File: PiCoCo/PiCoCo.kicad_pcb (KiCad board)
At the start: 2 copper layers, 98 x 65.2 mm, 42 parts, among them P1 COCO-CART, Q2 2N7002, U1 Pico 2, U10 SN74LVC8T245DW, U11 SN74LVC245AD, U12 SN74LVC245AD, U13 SN74LVC245AD, U14 AMS1117-3.3, U15 SN74LVC1G11

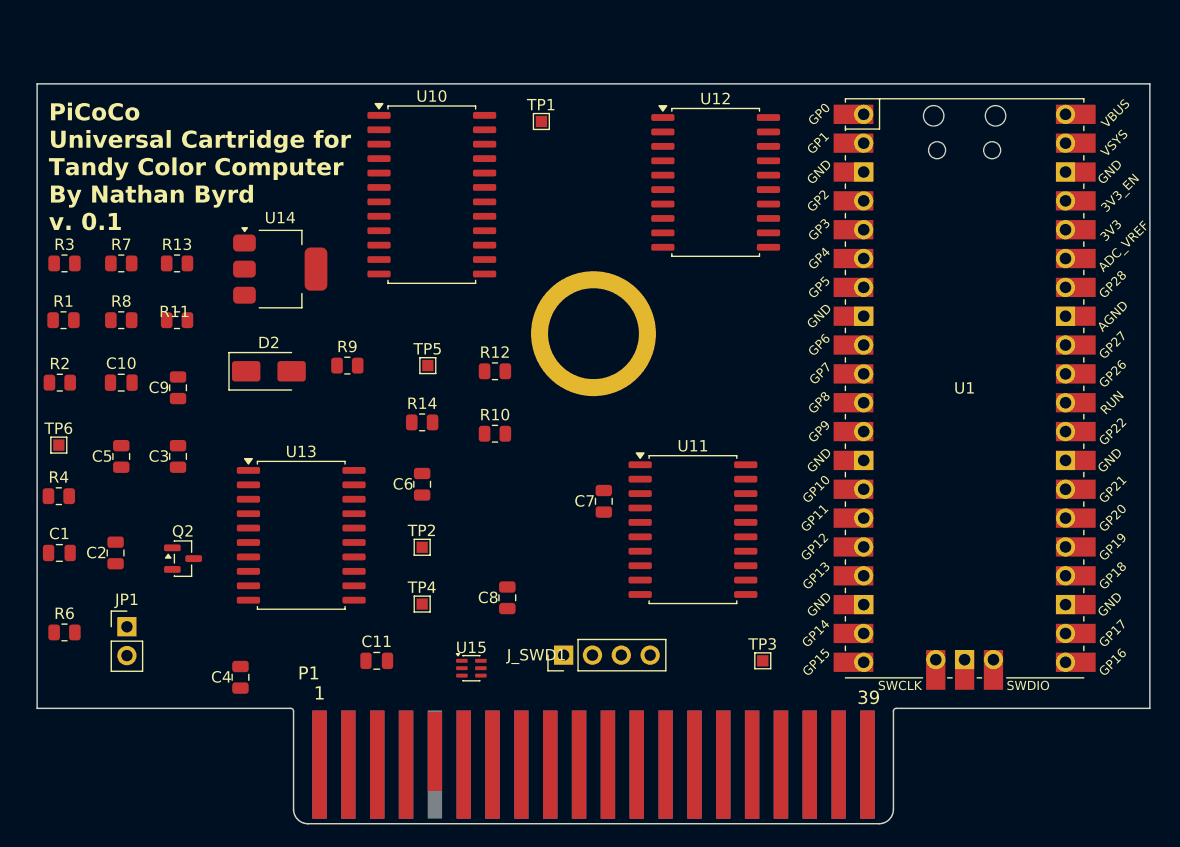
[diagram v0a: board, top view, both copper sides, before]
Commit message: kicad: v2.3 placement, antenna and HDMI rule areas, silkscreen
Placement table for the v2.3 refresh (Pico-Carrier module, LVC245/LVC00
buffers, sound stage, JP2/JP3, fiducials), antenna and HDMI-reserve
keepout zones, and silkscreen texts via place_pcb.py's add_board_extras().

Deviations from the task-4 brief, found via measured courtyard/pad
geometry after placement (not guessed):
- U14/C1 moved +/-3mm in x; D2's 7mm-wide courtyard didn't fit the
  brief's gap between them.
- Decoupling caps C4/C6/C7/C8 moved from y=84.0 to y=83.0; the buffer
  ICs' courtyard starts at y=85.35, so y=84.0 clipped it by ~0.35mm.
- JP3/C10 moved +8mm in x; at the brief's x=152 both sat inside U1's
  courtyard (ends x=155.52) and the antenna keepout (x 150.6..155.6).
- Sound stage (R19/C13/R20/C14/R21/R22/C15/TP7) regridded to 2 rows x
  4 cols right of U13 (courtyard ends x=187.93); the brief's single row
  put three parts inside both U13's courtyard and FID2's fiducial
  clearance.
- FID1 relocated twice (102.6/47.2 -> inside U1's own pad clearance;
  102.6/70.0 -> inside C12's 10.5x8.8mm courtyard) to 114.0/76.0, the
  first open spot found between C12 and R4/C2's row.

Known unresolved issue, needs a ruling: P1's MTG1 mounting-hole pad
(11mm pad / 8mm drill, baked into the shared COCO-CART footprint) sits
inside the v2.3 module's body corner regardless of U1's rotation (90 or
270), producing 3 hole_to_hole violations, several antenna-keepout
item_not_allowed hits, and ~11 net-shorting flags against U1's nearby
pins. This predates the v2.3 horizontal-module layout and can't be
fixed by nudging PLACEMENT; it needs either relocating MTG1 in the
footprint or accepting no mounting screw at that corner.

Also present, out of scope for this script: ~76 shorting_items flagged
between adjacent castellated pins on U1 itself (e.g. D0/D1) -- inherent
to the Pico-Carrier footprint's own pad-to-pad clearance vs. the
board's DRC clearance rule, a Task 1 footprint concern, not a
placement issue. 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
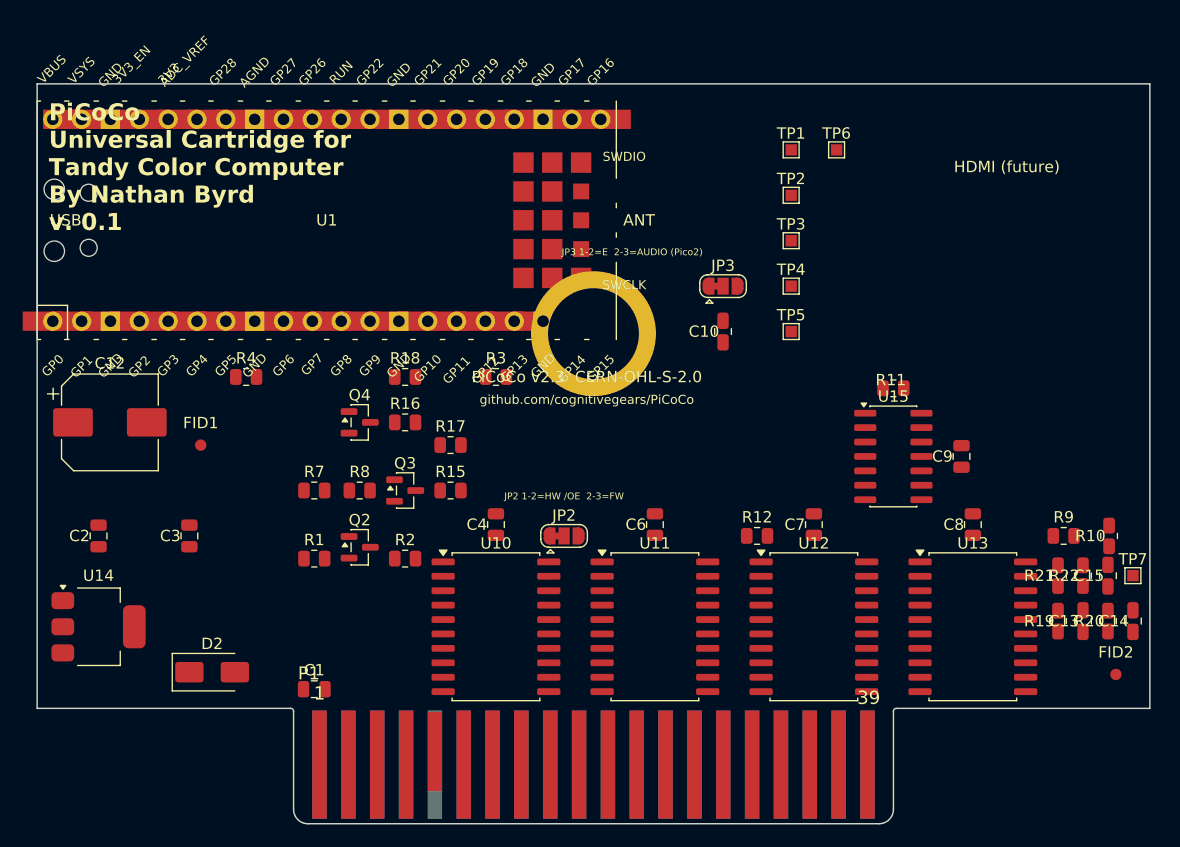
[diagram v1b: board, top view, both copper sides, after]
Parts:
- removed C11: 10uF, Capacitor_SMD:C_0805_2012Metric
- removed C5: 100nF, Capacitor_SMD:C_0805_2012Metric
- removed JP1: CART_EN, Connector_PinHeader_2.54mm:PinHeader_1x02_P2.54mm_Vertical
- removed J_SWD1: SWD, Connector_PinHeader_2.54mm:PinHeader_1x04_P2.54mm_Vertical
- removed R13, R14: 100, Resistor_SMD:R_0805_2012Metric
- removed R6: 4.7k, Resistor_SMD:R_0805_2012Metric
- added C12: 1000uF 6.3V, Capacitor_SMD:CP_Elec_8x10, F.Cu at (106.0, 74.0)
- added C13: 10nF, Capacitor_SMD:C_0805_2012Metric, F.Cu at (191.7, 91.5)
- added C14: 10nF, Capacitor_SMD:C_0805_2012Metric, F.Cu at (196.1, 91.5)
- added C15: 100nF, Capacitor_SMD:C_0805_2012Metric, F.Cu at (193.9, 87.5)
- added FID1: FID, Fiducial:Fiducial_1mm_Mask2mm, F.Cu at (114.0, 76.0)
- added FID2: FID, Fiducial:Fiducial_1mm_Mask2mm, F.Cu at (194.6, 96.2)
- added JP2: U10_OE_SEL, Jumper:SolderJumper-3_P1.3mm_Bridged12_RoundedPad1.0x1.5mm, F.Cu at (146.0, 84.0)
- added JP3: P34_SEL, Jumper:SolderJumper-3_P1.3mm_Bridged12_RoundedPad1.0x1.5mm, F.Cu at (160.0, 62.0)
- added Q3: 2N7002, Package_TO_SOT_SMD:SOT-23, F.Cu at (132.0, 80.0)
- added Q4: 2N7002, Package_TO_SOT_SMD:SOT-23, F.Cu at (128.0, 74.0)
- added R15: 100, Resistor_SMD:R_0805_2012Metric, F.Cu at (136.0, 80.0)
- added R16: 100, Resistor_SMD:R_0805_2012Metric, F.Cu at (132.0, 74.0)
- added R17: 100k, Resistor_SMD:R_0805_2012Metric, F.Cu at (136.0, 76.0)
- added R18: 100k, Resistor_SMD:R_0805_2012Metric, F.Cu at (132.0, 70.0)
- added R19: 1k, Resistor_SMD:R_0805_2012Metric, F.Cu at (189.5, 91.5)
- added R20: 1k, Resistor_SMD:R_0805_2012Metric, F.Cu at (193.9, 91.5)
- added R21: 2.2k, Resistor_SMD:R_0805_2012Metric, F.Cu at (189.5, 87.5)
- added R22: 1k, Resistor_SMD:R_0805_2012Metric, F.Cu at (191.7, 87.5)
- added TP7: SND_CART, TestPoint:TestPoint_Pad_1.0x1.0mm, F.Cu at (196.1, 87.5)
- TP5: value E_B -> E_BUF
- U1: value Pico 2 -> Pico 2 / RP2350B-Plus-W; footprint PiCoCo:RPi_Pico_SMD_TH -> PiCoCo:Pico-Carrier
- U10: value SN74LVC8T245DW -> SN74LVC245A; footprint Package_SO:SOIC-24W_7.5x15.4mm_P1.27mm -> Package_SO:SOIC-20W_7.5x12.8mm_P1.27mm
- U11, U12, U13: value SN74LVC245AD -> SN74LVC245A
- U15: value SN74LVC1G11 -> SN74LVC00A; footprint Package_TO_SOT_SMD:SOT-363_SC-70-6 -> Package_SO:SOIC-14_3.9x8.7mm_P1.27mm
- moved TP6 73.3 mm to (170.0, 50.0)
- moved C9 69.3 mm to (181.0, 77.0)
- moved R9 64.8 mm to (190.0, 84.0)
- moved R11 63.4 mm to (175.0, 71.0)
- moved U13 59.7 mm to (182.0, 92.0)
- moved U1 58.1 mm to (125.1, 56.2), turned to 90 degrees
- moved R10 54.8 mm to (194.0, 84.0), turned to 90 degrees
- moved C10 53.2 mm to (160.0, 66.0), turned to 90 degrees
- moved TP2 44.9 mm to (166.0, 54.0)
- moved TP4 42.9 mm to (166.0, 62.0)
- moved U15 41.6 mm to (175.0, 77.0)
- moved C8 41.5 mm to (182.0, 83.0)
- moved U12 40.1 mm to (168.0, 92.0)
- moved R3 39.3 mm to (140.0, 70.0)
- moved U10 38.5 mm to (140.0, 92.0)
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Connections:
- net A0_B renamed A0_BUF
- net A10_B renamed A10_BUF
- net A11_B renamed A11_BUF
- net A12_B renamed A12_BUF
- net A13_B renamed A13_BUF
- net A1_B renamed A1_BUF
- net A2_B renamed A2_BUF
- net A3_B renamed A3_BUF
- net A4_B renamed A4_BUF
- net A5_B renamed A5_BUF
- net A6_B renamed A6_BUF
- net A7_B renamed A7_BUF
- net A8_B renamed A8_BUF
- net A9_B renamed A9_BUF
- P1 pad 35: unconnected-(P1-SND-Pad35) -> SND_CART
- R9 pad 1: RESET_DBG -> RESET_BUF
- TP5 pad 1: E_B -> E_BUF
- U1 pad 34: E_B -> PICO_P34
- U10 pad 1: +3V3 -> RW_BUF
- U10 pad 10: D7_CART -> GND
- U10 pad 11: GND -> D7_CART
- U10 pad 12: GND -> D6_CART
- U10 pad 13: GND -> D5_CART
- U10 pad 14: D7 -> D4_CART
- U10 pad 15: D6 -> D3_CART
- U10 pad 16: D5 -> D2_CART
- U10 pad 17: D4 -> D1_CART
- U10 pad 18: D3 -> D0_CART
- U10 pad 19: D2 -> U10_OE
- U10 pad 2: RW_BUF -> D0
- U10 pad 20: D1 -> +3V3
- U10 pad 3: D0_CART -> D1
- U10 pad 4: D1_CART -> D2
- U10 pad 5: D2_CART -> D3
- U10 pad 6: D3_CART -> D4
- U10 pad 7: D4_CART -> D5
- U10 pad 8: D5_CART -> D6
- U10 pad 9: D6_CART -> D7
- U13 pad 12: RESET_DBG -> A15_BUF
- U13 pad 13: unconnected-(U13-B5-Pad13) -> A14_BUF
- U13 pad 14: unconnected-(U13-B4-Pad14) -> RESET_BUF
- U13 pad 15: unconnected-(U13-B3-Pad15) -> SLENB_BUF
- U13 pad 16: unconnected-(U13-B2-Pad16) -> Q_BUF
- U13 pad 17: E_B -> E_BUF
- U13 pad 6: HALT_CART -> RESET_CART
- U13 pad 7: NMI_CART -> A14_CART
- U13 pad 8: RESET_CART -> A15_CART
- U13 pad 9: CART_CART -> GND
- U15 pad 2: GND -> SCS_BUF
- U15 pad 3: SCS_BUF -> SEL_N
- U15 pad 4: OE_BUS_RAW -> SEL_N
- U15 pad 5: +3V3 -> E_BUF
- U15 pad 6: E_B -> OE_BUS_RAW
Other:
- board text added: "HDMI (future)"
- board text added: "JLCJLCJLCJLC"
- board text added: "JP2 1-2=HW /OE 2-3=FW"
- board text added: "JP3 1-2=E 2-3=AUDIO (Pico2)"
- board text added: "PiCoCo v2.3 CERN-OHL-S-2.0"
- board text added: "github.com/cognitivegears/PiCoCo"
- board text added: "no parts under module"

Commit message: kicad: v2.3 placement on the re-synced board, DRC error-free before routing
Ruling (b) applied: place_pcb.py now SETS every placed footprint's pad,
fp_text and property angles to the footprint's own target rotation directly
(not delta-added to whatever was on file), since every part on this board
has zero relative pad rotation in its library copy. This self-heals stale
angles regardless of whether the footprint's own rotation is changing this
run (the R10/C10 concern from the prior round), while leaving
already-correct footprints byte-identical (angle only rewritten when it
differs from the target). Verified with unit tests covering all four cases:
already-at-target no-op, stale-angle self-heal, target-0 stays-absent, and
target-0 corrects a stale nonzero angle.

Also fixed add_board_extras()'s zone idempotency: it previously matched an
existing zone by name only, so a changed EXTRAS polygon (see below) would
never actually get written on rerun. It now replaces a stale zone (name
matches, content doesn't) instead of skipping it.

Ran placement on the real re-synced board (confirmed first: Pico-Carrier
present, MTG1 absent, SWDIO absent, fingers trimmed to 8.67mm): 53
footprints moved, 0 missing. Pad 1 (USB) at x=100.97, pad 20 (antenna) at
x=149.23, matching spec.

DRC (--severity-all, sandbox-disabled retry for the known kicad-cli crash)
went from 1 error + 87 shorting_items-style noise (last round, before this
fix) to 0 errors other than the expected 179 unconnected_items. Two
follow-on zone fixes were needed to get there:
- antenna_keepout's left edge moved from the module's nominal x=150.6 to
  x=151.3: pad 20/21's castellated copper legitimately overhangs the
  nominal edge by ~0.4mm (measured), which a zone starting exactly at the
  edge clips.
- Dropped "footprints not_allowed" from that zone: it was flagging U1's own
  courtyard, which legitimately extends into the antenna area by design;
  the zone's real intent (keeping other components' copper out) is cov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
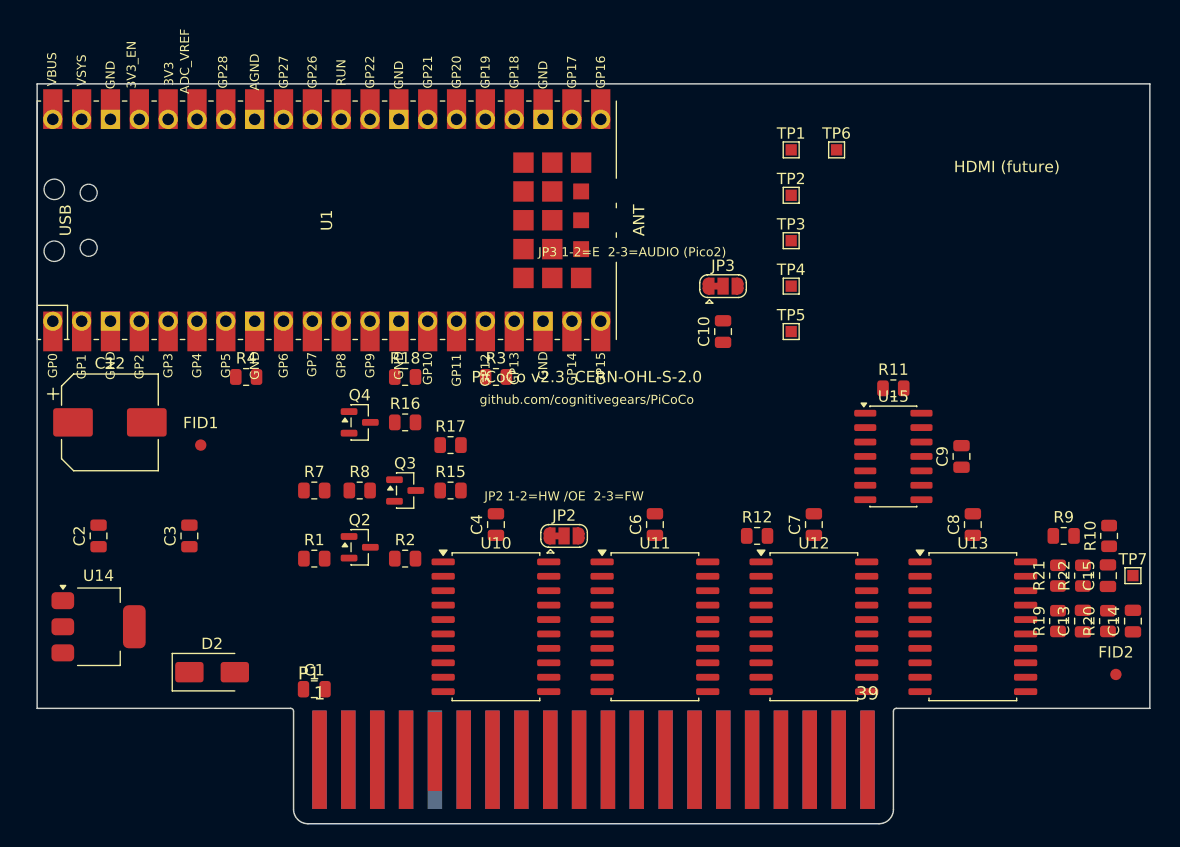
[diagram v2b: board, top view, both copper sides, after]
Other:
- board text removed: "PiCoCo Universal Cartridge for Tandy Color Computer By Nathan Byrd v. 0.1"

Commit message: kicad: placement fixes from review (text angles by delta, legends off the module, FID1, text replace)
F1 IMPORTANT: ruling (b) from the prior round was wrong for fp_text/property
angles. Pico-Carrier's 40 pin labels are 45deg relative to the footprint,
and reference/value auto-text is 180deg relative on some parts; setting
every child to the footprint's absolute target angle flattened those
relative offsets (most of the prior round's silk warnings). New rule:
pads -> SET to the target rotation (unchanged, correct for pads on this
board). fp_text/property -> ADD (target - old_footprint_rotation) mod 360,
preserving whatever relative angle KiCad wrote them with at sync time. Pad
self-check kept; text angles are not self-checked (per ruling, since their
correct value depends on each part's own library-relative angle, not a
single board-wide invariant).

F2: JP3's legend was inside U1's courtyard/pad grid. At 0.8mm the full
string measures 20.5mm wide (measured via pcbnew) -- wider than the 16.6mm
corridor between U1's courtyard (ends x=155.52) and the HDMI reserve
(starts x=172.6), so a single line always bled into either U1 or R11
(which sits just past x=172.6). Split into two lines ("JP3 1-2=E" /
"2-3=AUDIO (Pico2)"), both fitting the corridor, in the clear y=68.5..71.5
band (below C10, above R12/U12's row).

F3: add_board_extras()'s text/zone dedupe matched by exact string, so a
changed position/size/layer never landed on an existing board. Added
_upsert_item(), shared by both zones and texts: replaces an item matching
its identity marker (a zone's name, a gr_text's content) if the content
differs, instead of skipping.

F4: FID1 moved to (102.6, 80.0) per review (measured clear with 1.5mm
margin there, and lengthens the fiducial diagonal vs the prior (114, 76)).

F5: "PiCoCo v2.3 CERN-OHL-S-2.0" and the URL moved to B.SilkS (mirrored,
like the JLC text), centred in the empty back area (x=150, y=75/78) -- on
the front they crossed U1's lower pin labels and R3. JP2's 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
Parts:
- moved FID1 12.1 mm to (102.6, 80.0)
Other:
- board text added: "2-3=AUDIO (Pico2)"
- board text added: "JP3 1-2=E"
- board text removed: "JP3 1-2=E 2-3=AUDIO (Pico2)"
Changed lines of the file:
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@@
 	(footprint "Fiducial:Fiducial_1mm_Mask2mm"
 		(layer "F.Cu")
-		(at 114.000 76.000)
+		(at 102.600 80.000)
 		(descr "Fiducial, circular marking, 1mm bare copper, 2mm soldermask opening (Level A)")
 		(tags "fiducial")
@@
     (effects (font (size 1.0 1.0) (thickness 0.15)))
   )
-  (gr_text "PiCoCo v2.3  CERN-OHL-S-2.0" (at 148.0 70.0 0) (layer "F.SilkS")
-    (effects (font (size 1.0 1.0) (thickness 0.15)))
-  )
-  (gr_text "github.com/cognitivegears/PiCoCo" (at 148.0 72.0 0) (layer "F.SilkS")
-    (effects (font (size 0.8 0.8) (thickness 0.12)))
-  )
   (gr_text "JLCJLCJLCJLC" (at 110.0 62.0 0) (layer "B.SilkS")
     (effects (font (size 1.0 1.0) (thickness 0.15)) (justify mirror))
-  )
-  (gr_text "JP2 1-2=HW /OE  2-3=FW" (at 146.0 80.5 0) (layer "F.SilkS")
-    (effects (font (size 0.8 0.8) (thickness 0.12)))
-  )
-  (gr_text "JP3 1-2=E  2-3=AUDIO (Pico2)" (at 152.0 59.0 0) (layer "F.SilkS")
-    (effects (font (size 0.8 0.8) (thickness 0.12)))
   )
   (gr_text "no parts under module" (at 125.0 62.0 0) (layer "F.Fab")
@@
     (polygon (pts (xy 151.300 45.700) (xy 155.600 45.700) (xy 155.600 66.700) (xy 151.300 66.700)))
   )
+  (gr_text "PiCoCo v2.3  CERN-OHL-S-2.0" (at 150.0 75.0 0) (layer "B.SilkS")
+    (effects (font (size 1.0 1.0) (thickness 0.15)) (justify mirror))
+  )
+  (gr_text "github.com/cognitivegears/PiCoCo" (at 150.0 78.0 0) (layer "B.SilkS")
+    (effects (font (size 0.8 0.8) (thickness 0.12)) (justify mirror))
+  )
+  (gr_text "JP2 1-2=HW /OE  2-3=FW" (at 152.0 80.5 0) (layer "F.SilkS")
+    (effects (font (size 0.8 0.8) (thickness 0.12)))
+  )
+  (gr_text "JP3 1-2=E" (at 164.0 69.0 0) (layer "F.SilkS")
+    (effects (font (size 0.8 0.8) (thickness 0.12)))
+  )
+  (gr_text "2-3=AUDIO (Pico2)" (at 164.0 71.0 0) (layer "F.SilkS")
+    (effects (font (size 0.8 0.8) (thickness 0.12)))
+  )
 )
